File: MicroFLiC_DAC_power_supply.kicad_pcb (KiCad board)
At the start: 2 copper layers, 49.8 x 49.8 mm, 69 parts, among them P1 1x2 socket strip, P2 1x2 header strip, P3 2x4 socket strip, U1 AP1117E50, U2 AP1117, U3 AP1117, U4 LM317, U5 LM317

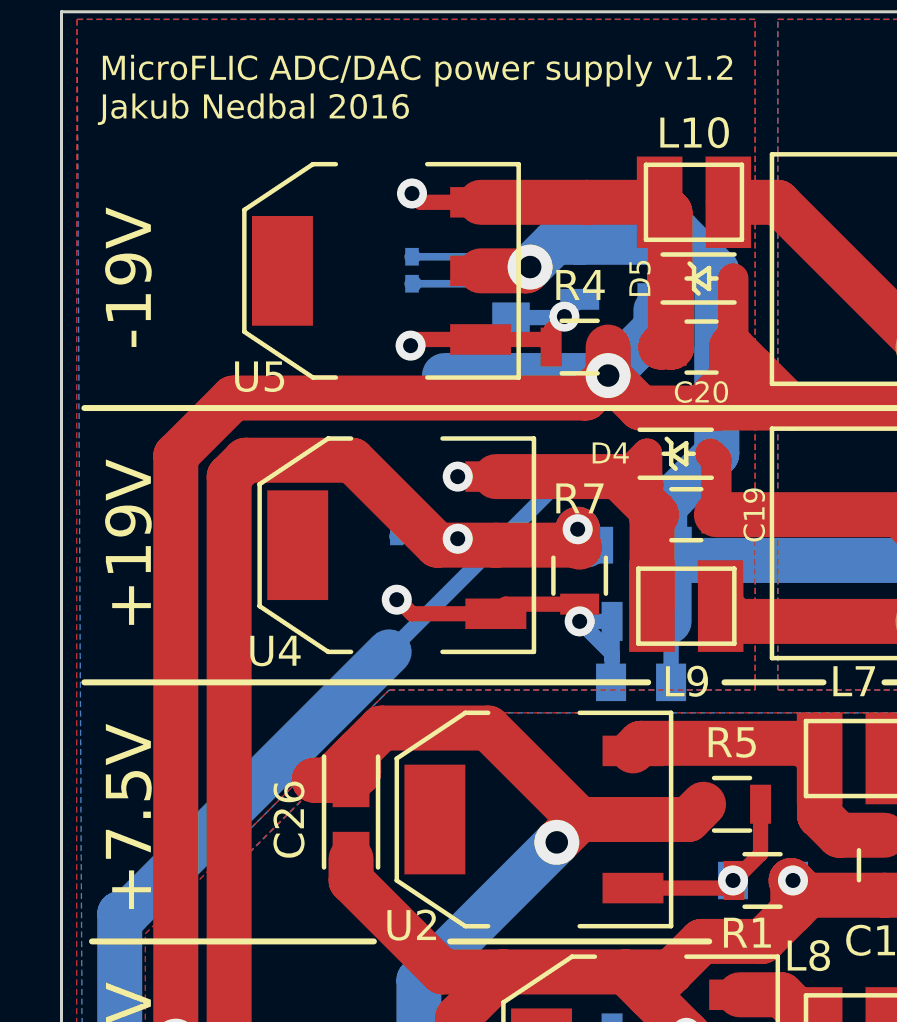
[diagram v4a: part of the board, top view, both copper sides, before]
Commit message: Changed SOD-323 packages for larger pads.
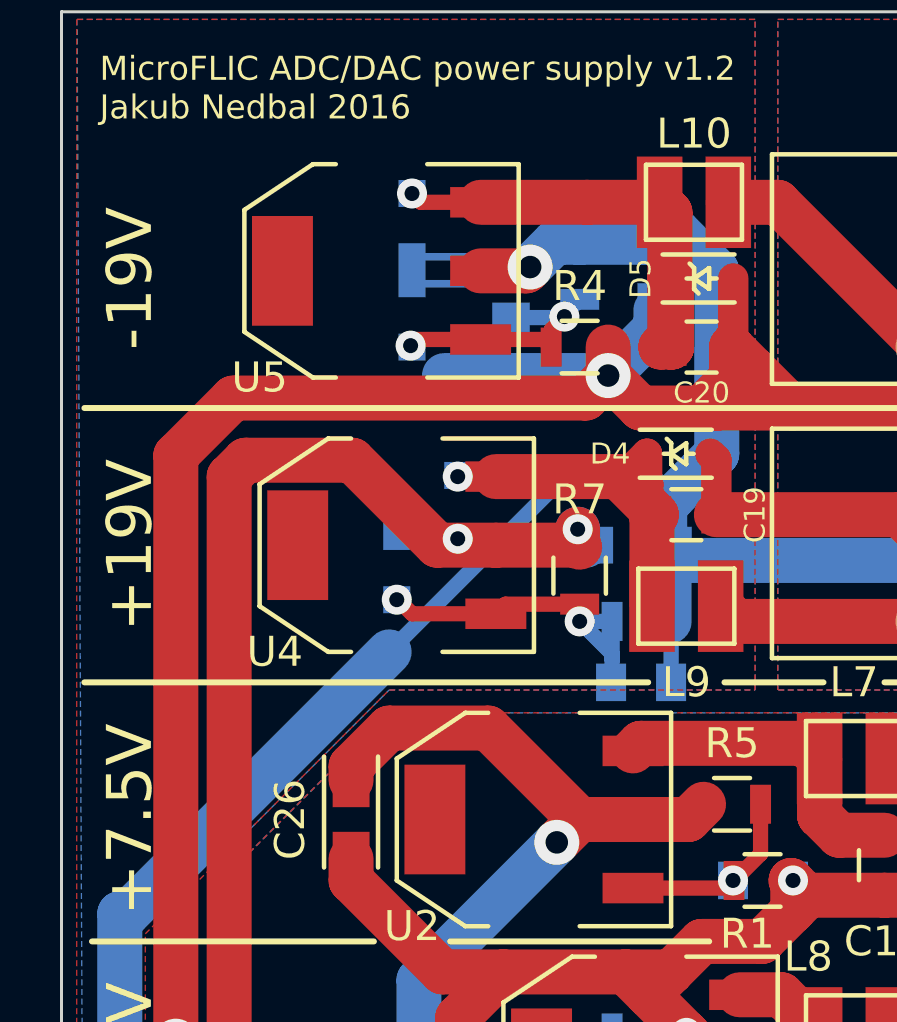
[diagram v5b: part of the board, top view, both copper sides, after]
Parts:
- D6, D7, D8, D9: footprint Diodes_SMD:SOD-323 -> jakub:SOD-323
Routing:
- net /+7.5V: track 43.8 -> 40.2 mm
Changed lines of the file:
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@@
-(kicad_pcb (version 4) (host pcbnew "(2015-12-10 BZR 6367)-product")
+(kicad_pcb (version 4) (host pcbnew 4.0.2-4+6225~38~ubuntu14.04.1-stable)
   (general
     (links 130)
@@
     (thickness 1.6)
     (drawings 38)
-    (tracks 451)
+    (tracks 446)
     (zones 0)
     (modules 69)
@@
   (layers
     (0 F.Cu signal)
-    (31 B.Cu signal)
+    (31 B.Cu signal hide)
     (32 B.Adhes user)
     (33 F.Adhes user)
@@
     (pad_to_mask_clearance 0)
     (aux_axis_origin 100.076 149.86)
-    (visible_elements FFFFFF7F)
+    (visible_elements FFFEFF7F)
     (pcbplotparams
       (layerselection 0x010f0_80000001)
@@
     (tags "Tantal Capacitor Size-A EIA-3216 reflow")
     (attr smd)
-    (fp_text reference C28 (at 0 -2.032) (layer B.SilkS)
+    (fp_text reference C28 (at 0 -1.778) (layer B.SilkS)
       (effects (font (size 1 1) (thickness 0.15)) (justify mirror))
     )
@@
     (tags "capacitor 0805")
     (attr smd)
-    (fp_text reference C21 (at 0 2.1) (layer B.SilkS)
+    (fp_text reference C21 (at -0.016 1.778) (layer B.SilkS)
       (effects (font (size 1 1) (thickness 0.15)) (justify mirror))
     )
@@
     (tags "capacitor 0805")
     (attr smd)
-    (fp_text reference C23 (at 3.286 0) (layer B.SilkS)
+    (fp_text reference C23 (at -0.016 1.778) (layer B.SilkS)
       (effects (font (size 1 1) (thickness 0.15)) (justify mirror))
     )
@@
     (tags "capacitor 0805")
     (attr smd)
-    (fp_text reference C24 (at 2.524 -0.508 360) (layer B.SilkS)
+    (fp_text reference C24 (at 2.524 0 360) (layer B.SilkS)
       (effects (font (size 1 1) (thickness 0.15)) (justify mirror))
     )
@@
     )
   )
-  (module Diodes_SMD:SOD-323 (layer B.Cu)
+  (module jakub:SOD-323 (layer B.Cu)
     (at 113.284 116.586 270)
     (descr SOD-323)
     (tags SOD-323)
     (attr smd)
-    (fp_text reference D6 (at -2.286 0.508 360) (layer B.SilkS)
-      (effects (font (size 1 1) (thickness 0.15)) (justify mirror))
-    )
-    (fp_text value 1N4148 (at 0.1 -1.9 270) (layer B.Fab) hide
+    (fp_text reference D6 (at -0.762 1.524 270) (layer B.SilkS)
+      (effects (font (size 1 1) (thickness 0.15)) (justify mirror))
+    )
+    (fp_text value 1N4148 (at 0.1 -1.9 270) (layer B.Fab)
       (effects (font (size 1 1) (thickness 0.15)) (justify mirror))
     )
@@
     (fp_line (start -1.3 -0.8) (end 1.1 -0.8) (layer B.SilkS) (width 0.15))
     (fp_line (start -1.3 0.8) (end 1.1 0.8) (layer B.SilkS) (width 0.15))
-    (pad 1 smd rect (at -1.055 0 270) (size 0.59 0.45) (layers B.Cu B.Paste B.Mask)
+    (pad 1 smd rect (at -1.055 0 270) (size 0.9 0.9) (layers B.Cu B.Paste B.Mask)
       (net 6 /+24_ID))
-    (pad 2 smd rect (at 1.055 0 270) (size 0.59 0.45) (layers B.Cu B.Paste B.Mask)
+    (pad 2 smd rect (at 1.055 0 270) (size 0.9 0.9) (layers B.Cu B.Paste B.Mask)
       (net 28 /+19V))
     (model jakub.3dshapes/diodes/sod323.wrl
@@
     )
   )
-  (module Diodes_SMD:SOD-323 (layer B.Cu)
+  (module jakub:SOD-323 (layer B.Cu)
     (at 111.76 107.188 270)
     (descr SOD-323)
     (tags SOD-323)
     (attr smd)
-    (fp_text reference D7 (at -2.247 0 360) (layer B.SilkS)
-      (effects (font (size 1 1) (thickness 0.15)) (justify mirror))
-    )
-    (fp_text value 1N4148 (at 0.1 -1.9 270) (layer B.Fab) hide
+    (fp_text reference D7 (at 0 1.524 270) (layer B.SilkS)
+      (effects (font (size 1 1) (thickness 0.15)) (justify mirror))
+    )
+    (fp_text value 1N4148 (at 0.1 -1.9 270) (layer B.Fab)
       (effects (font (size 1 1) (thickness 0.15)) (justify mirror))
     )
@@
     (fp_line (start -1.3 -0.8) (end 1.1 -0.8) (layer B.SilkS) (width 0.15))
     (fp_line (start -1.3 0.8) (end 1.1 0.8) (layer B.SilkS) (width 0.15))
-    (pad 1 smd rect (at -1.055 0 270) (size 0.59 0.45) (layers B.Cu B.Paste B.Mask)
+    (pad 1 smd rect (at -1.055 0 270) (size 0.9 0.9) (layers B.Cu B.Paste B.Mask)
       (net 23 /+24_IE))
-    (pad 2 smd rect (at 1.055 0 270) (size 0.59 0.45) (layers B.Cu B.Paste B.Mask)
+    (pad 2 smd rect (at 1.055 0 270) (size 0.9 0.9) (layers B.Cu B.Paste B.Mask)
       (net 26 /19V_GND))
     (model jakub.3dshapes/diodes/sod323.wrl
@@
     )
   )
-  (module Diodes_SMD:SOD-323 (layer B.Cu)
+  (module jakub:SOD-323 (layer B.Cu)
     (at 111.252 118.618 270)
     (descr SOD-323)
     (tags SOD-323)
     (attr smd)
-    (fp_text reference D8 (at 2.286 0 360) (layer B.SilkS)
-      (effects (font (size 1 1) (thickness 0.15)) (justify mirror))
-    )
-    (fp_text value 1N4148 (at 0.1 -1.9 270) (layer B.Fab) hide
+    (fp_text reference D8 (at 0 1.524 270) (layer B.SilkS)
+      (effects (font (size 1 1) (thickness 0.15)) (justify mirror))
+    )
+    (fp_text value 1N4148 (at 0.1 -1.9 270) (layer B.Fab)
       (effects (font (size 1 1) (thickness 0.15)) (justify mirror))
     )
@@
     (fp_line (start -1.3 -0.8) (end 1.1 -0.8) (layer B.SilkS) (width 0.15))
     (fp_line (start -1.3 0.8) (end 1.1 0.8) (layer B.SilkS) (width 0.15))
-    (pad 1 smd rect (at -1.055 0 270) (size 0.59 0.45) (layers B.Cu B.Paste B.Mask)
+    (pad 1 smd rect (at -1.055 0 270) (size 0.9 0.9) (layers B.Cu B.Paste B.Mask)
       (net 28 /+19V))
-    (pad 2 smd rect (at 1.055 0 270) (size 0.59 0.45) (layers B.Cu B.Paste B.Mask)
+    (pad 2 smd rect (at 1.055 0 270) (size 0.9 0.9) (layers B.Cu B.Paste B.Mask)
       (net 19 /FB_D))
     (model jakub.3dshapes/diodes/sod323.wrl
@@
     )
   )
-  (module Diodes_SMD:SOD-323 (layer B.Cu)
+  (module jakub:SOD-323 (layer B.Cu)
     (at 111.76 110.197 270)
     (descr SOD-323)
     (tags SOD-323)
     (attr smd)
-    (fp_text reference D9 (at 2.325 0 360) (layer B.SilkS)
-      (effects (font (size 1 1) (thickness 0.15)) (justify mirror))
-    )
-    (fp_text value 1N4148 (at 0.1 -1.9 270) (layer B.Fab) hide
+    (fp_text reference D9 (at 0 1.524 270) (layer B.SilkS)
+      (effects (font (size 1 1) (thickness 0.15)) (justify mirror))
+    )
+    (fp_text value 1N4148 (at 0.1 -1.9 270) (layer B.Fab)
       (effects (font (size 1 1) (thickness 0.15)) (justify mirror))
     )
@@
     (fp_line (start -1.3 -0.8) (end 1.1 -0.8) (layer B.SilkS) (width 0.15))
     (fp_line (start -1.3 0.8) (end 1.1 0.8) (layer B.SilkS) (width 0.15))
-    (pad 1 smd rect (at -1.055 0 270) (size 0.59 0.45) (layers B.Cu B.Paste B.Mask)
+    (pad 1 smd rect (at -1.055 0 270) (size 0.9 0.9) (layers B.Cu B.Paste B.Mask)
       (net 26 /19V_GND))
-    (pad 2 smd rect (at 1.055 0 270) (size 0.59 0.45) (layers B.Cu B.Paste B.Mask)
+    (pad 2 smd rect (at 1.055 0 270) (size 0.9 0.9) (layers B.Cu B.Paste B.Mask)
       (net 20 /FB_E))
     (model jakub.3dshapes/diodes/sod323.wrl
@@
   (segment (start 110.744 142.24) (end 109.728 143.256) (width 1.5) (layer F.Cu) (net 8))
   (segment (start 109.728 143.256) (end 109.728 143.978) (width 1.5) (layer F.Cu) (net 8))
+  (segment (start 109.728 125.69) (end 109.728 125.222) (width 1.5) (layer F.Cu) (net 9))
+  (segment (start 109.728 125.222) (end 110.998 123.952) (width 1.5) (layer F.Cu) (net 9))
+  (segment (start 110.998 123.952) (end 114.3 123.952) (width 1.5) (layer F.Cu) (net 9))
+  (segment (start 114.3 123.952) (end 117.348 127) (width 1.5) (layer F.Cu) (net 9))
   (segment (start 116.586 127.762) (end 117.348 127) (width 1.5) (layer F.Cu) (net 9))
   (segment (start 111.99001 143.366392) (end 111.99001 132.35799) (width 1.5) (layer B.Cu) (net 9))
@@
   (segment (start 119.126 127) (end 120.97 127) (width 1.5) (layer F.Cu) (net 9))
   (segment (start 119.126 127) (end 117.348 127) (width 1.5) (layer F.Cu) (net 9))
-  (segment (start 117.348 127) (end 114.3 123.952) (width 1.5) (layer F.Cu) (net 9))
-  (segment (start 114.3 123.952) (end 110.744 123.952) (width 1.5) (layer F.Cu) (net 9))
-  (segment (start 110.744 123.952) (end 109.982 124.714) (width 1.5) (layer F.Cu) (net 9))
-  (segment (start 109.982 124.714) (end 109.982 125.436) (width 1.5) (layer F.Cu) (net 9))
-  (segment (start 108.498 125.69) (end 109.006 125.69) (width 1.5) (layer F.Cu) (net 9))
-  (segment (start 109.006 125.69) (end 109.982 124.714) (width 1.5) (layer F.Cu) (net 9))
-  (segment (start 109.982 125.436) (end 109.728 125.69) (width 1.5) (layer F.Cu) (net 9))
-  (segment (start 108.498 125.69) (end 109.728 125.69) (width 1.5) (layer F.Cu) (net 9))
-  (segment (start 109.982 124.714) (end 109.728 124.968) (width 1.5) (layer F.Cu) (net 9))
   (segment (start 120.97 127) (end 121.478 126.492) (width 1.5) (layer F.Cu) (net 9))
   (segment (start 128.778 143.256) (end 124.589 143.256) (width 1.5) (layer F.Cu) (net 10))
